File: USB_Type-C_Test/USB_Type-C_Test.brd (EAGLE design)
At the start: 32.5 x 65 mm, 51 parts, among them J1 105450-0101, U1 P8X32A-Q44, U2 FT230XQ-R, U4 CAT24C512WI-GT3, U6 NCP1117LPST33T3G, U7 IRLML6401TRPBF, X1 ABMM-6.000MHZ-B2-T

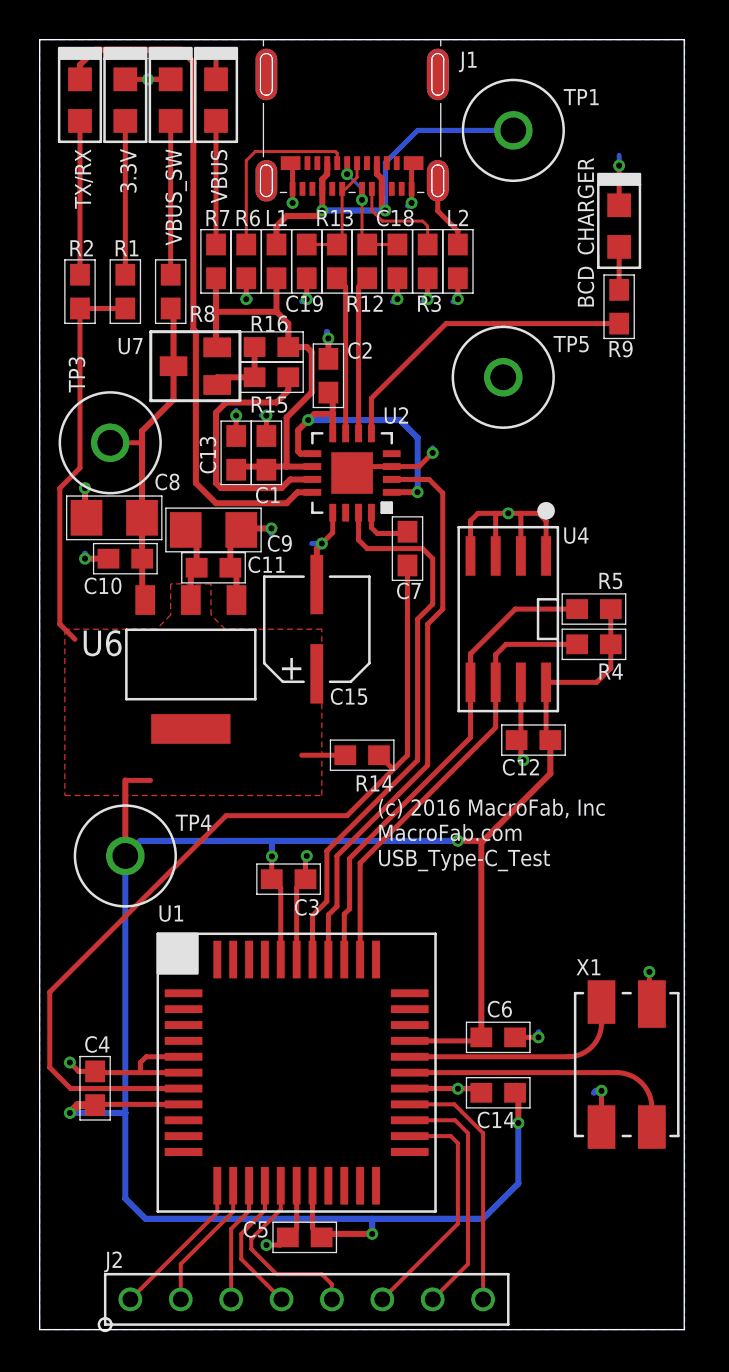
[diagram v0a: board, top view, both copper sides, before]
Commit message: Fixing the Type C connector.
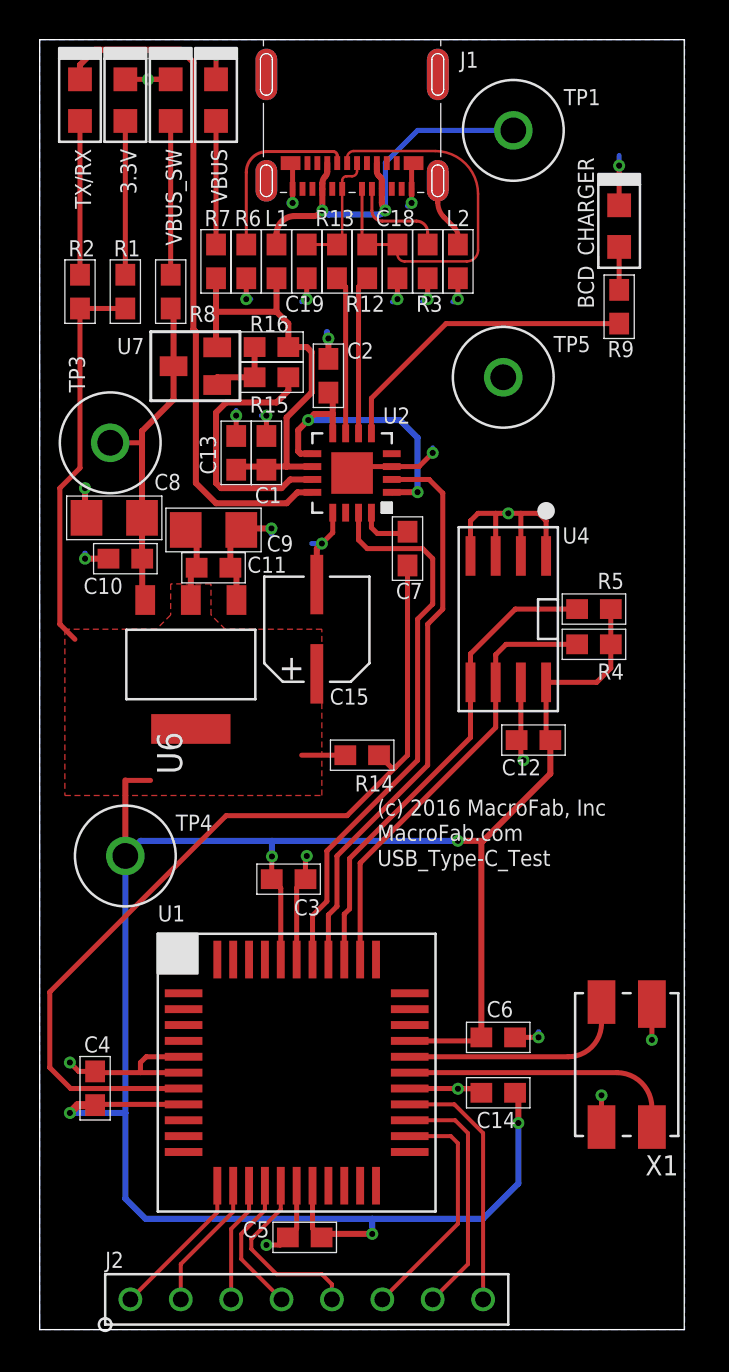
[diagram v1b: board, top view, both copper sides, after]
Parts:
- FRAME1: value MF_FRAMEDEFAULT -> (none)
- TP1, TP3, TP4, TP5: value 5115 -> (none)
- turned U6 to 270 degrees
- turned X1 to 180 degrees
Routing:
- net D+: track 6.60 -> 20.1 mm, vias 2 -> 0
- net GND: track 85.7 -> 85.1 mm

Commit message: Finishing up the board design.
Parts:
- removed R6: 5.1K, PP_Passives:0603
- moved C18 0.76 mm to (18.8, 53.8)
- moved C19 0.76 mm to (12.7, 53.8)
- moved L1 0.76 mm to (11.2, 53.8)
- moved L2 0.76 mm to (21.8, 53.8)
- moved R3 0.76 mm to (20.3, 53.8)
- moved R13 0.51 mm to (14.5, 53.8)
- moved R12 0.51 mm to (17.0, 53.8)
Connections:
- removed net N$5: J1.B5, R6.1
- net GND: no longer R6.2
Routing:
- net N$5: track 9.12 -> 0.00 mm
- net D-: track 6.21 -> 14.1 mm, vias 0 -> 2
- net D+: track 20.1 -> 14.1 mm, vias 0 -> 2
- net VBUS: track 21.1 -> 25.7 mm, vias 2 -> 0
- net GND: track 85.1 -> 83.4 mm, vias 27 -> 26
- net N$4: track 3.53 -> 4.28 mm
